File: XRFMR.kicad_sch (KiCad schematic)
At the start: 1 part, among them T1 PL140-105L_

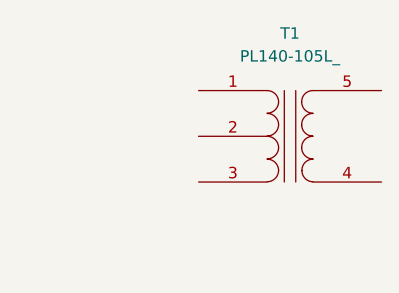
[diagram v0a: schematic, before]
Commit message: Initial pass of component placement complete. Added test points and i2c headers, also changed 12V input to terminal block
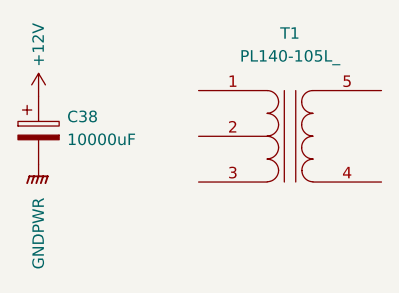
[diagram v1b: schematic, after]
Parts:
- added C38: 10000uF, Capacitor_THT:CP_Radial_D22.0mm_P10.00mm_SnapIn, symbol Device:C_Polarized
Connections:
- new net +12V: C38.1
- new net GNDPWR: C38.2
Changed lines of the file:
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@@
 (kicad_sch (version 20230121) (generator eeschema)
   (paper "A4")
+  (symbol (lib_id "power:+12V") (at 99.695 76.2 0) (unit 1)
+    (in_bom yes) (on_board yes) (dnp no)
+    (property "Reference" "#PWR060" (at 99.695 80.01 0)
+      (effects (font (size 1.27 1.27)) hide)
+    )
+    (property "Value" "+12V" (at 99.695 70.485 90)
+      (effects (font (size 1.27 1.27)))
+    )
+    (property "Footprint" "" (at 99.695 76.2 0)
+      (effects (font (size 1.27 1.27)) hide)
+    )
+    (property "Datasheet" "" (at 99.695 76.2 0)
+      (effects (font (size 1.27 1.27)) hide)
+    )
+    (pin "1")
+    (instances
+      (project "AMF-Generator"
+        (path "/c3df021c-646c-4a68-ac14-a081c2121d02"
+          (reference "#PWR060") (unit 1)
+        )
+      )
+      (project "XRFMR"
+        (path "/ff4be573-00c7-4055-9753-177d4ee7e88e"
+          (reference "#PWR01") (unit 1)
+        )
+      )
+    )
+  )
+  (symbol (lib_id "Device:C_Polarized") (at 99.695 80.01 0) (unit 1)
+    (in_bom yes) (on_board yes) (dnp no) (fields_autoplaced)
+    (property "Reference" "C38" (at 102.87 78.486 0)
+      (effects (font (size 1.27 1.27)) (justify left))
+    )
+    (property "Value" "10000uF" (at 102.87 81.026 0)
+      (effects (font (size 1.27 1.27)) (justify left))
+    )
+    (property "Footprint" "Capacitor_THT:CP_Radial_D22.0mm_P10.00mm_SnapIn" (at 100.6602 83.82 0)
+      (effects (font (size 1.27 1.27)) hide)
+    )
+    (property "Datasheet" "~" (at 99.695 80.01 0)
+      (effects (font (size 1.27 1.27)) hide)
+    )
+    (pin "1")
+    (pin "2")
+    (instances
+      (project "AMF-Generator"
+        (path "/c3df021c-646c-4a68-ac14-a081c2121d02"
+          (reference "C38") (unit 1)
+        )
+      )
+      (project "XRFMR"
+        (path "/ff4be573-00c7-4055-9753-177d4ee7e88e"
+          (reference "C1") (unit 1)
+        )
+      )
+    )
+  )
+  (symbol (lib_id "power:GNDPWR") (at 99.695 83.82 0) (unit 1)
+    (in_bom yes) (on_board yes) (dnp no)
+    (property "Reference" "#PWR061" (at 99.695 88.9 0)
+      (effects (font (size 1.27 1.27)) hide)
+    )
+    (property "Value" "GNDPWR" (at 99.695 91.44 90)
+      (effects (font (size 1.27 1.27)))
+    )
+    (property "Footprint" "" (at 99.695 85.09 0)
+      (effects (font (size 1.27 1.27)) hide)
+    )
+    (property "Datasheet" "" (at 99.695 85.09 0)
+      (effects (font (size 1.27 1.27)) hide)
+    )
+    (pin "1")
+    (instances
+      (project "AMF-Generator"
+        (path "/c3df021c-646c-4a68-ac14-a081c2121d02"
+          (reference "#PWR061") (unit 1)
+        )
+      )
+      (project "XRFMR"
+        (path "/ff4be573-00c7-4055-9753-177d4ee7e88e"
+          (reference "#PWR02") (unit 1)
+        )
+      )
+    )
+  )
   (symbol (lib_id "Device:Transformer_SP_1S") (at 127.635 80.645 0) (unit 1)
     (in_bom yes) (on_board yes) (dnp no)
@@
         )
       )
+      (project "XRFMR"
+        (path "/ff4be573-00c7-4055-9753-177d4ee7e88e"
+          (reference "T1") (unit 1)
+        )
+      )
     )
   )
+  (sheet_instances
+    (path "/" (page "1"))
+  )
 )
